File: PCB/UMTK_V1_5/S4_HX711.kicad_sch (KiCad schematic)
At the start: 13 parts, among them Q9 Q_PNP_BEC, U1 HX711

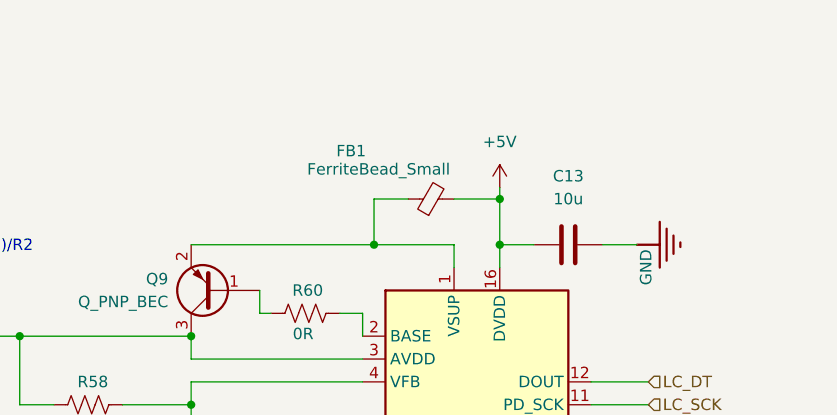
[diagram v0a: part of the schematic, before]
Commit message: Updated Schematics
Done: 7 Seg, Power, Motor, Slide, HX711
To Do: Arduino
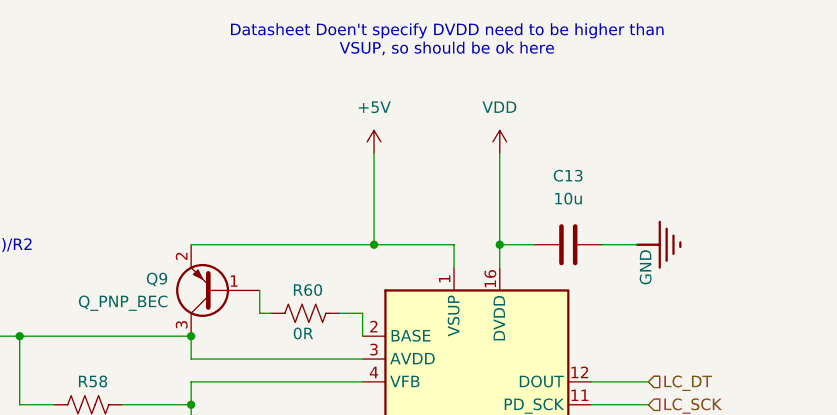
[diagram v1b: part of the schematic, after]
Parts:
- removed FB1: FerriteBead_Small, symbol Device:FerriteBead_Small
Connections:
- net +5V: now also Q9.2 (E), U1.1 (VSUP); no longer C13.1, U1.16 (DVDD)
- new net VDD: C13.1, U1.16 (DVDD)
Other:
- note added: "Datasheet Doen't specify DVDD need to be higher than VSUP, so should be ok here"
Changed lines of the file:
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@@
 	(paper "A4")
-	(junction
-		(at 167.64 82.55)
-		(diameter 0)
-		(color 0 0 0 0)
-	)
 	(junction
 		(at 115.57 127)
@@
 	(wire
 		(pts
-			(xy 167.64 82.55) (xy 167.64 87.63)
-		)
-		(stroke
-			(width 0)
-			(type default)
-		)
-	)
-	(wire
-		(pts
 			(xy 146.05 113.03) (xy 152.4 113.03)
 		)
@@
 	(wire
 		(pts
-			(xy 157.48 82.55) (xy 153.67 82.55)
-		)
-		(stroke
-			(width 0)
-			(type default)
-		)
-	)
-	(wire
-		(pts
 			(xy 88.9 97.79) (xy 100.33 97.79)
 		)
@@
 	(wire
 		(pts
-			(xy 162.56 82.55) (xy 167.64 82.55)
-		)
-		(stroke
-			(width 0)
-			(type default)
-		)
-	)
-	(wire
-		(pts
-			(xy 167.64 81.28) (xy 167.64 82.55)
+			(xy 153.67 77.47) (xy 153.67 87.63)
 		)
 		(stroke
@@
 	(wire
 		(pts
-			(xy 153.67 82.55) (xy 153.67 87.63)
-		)
-		(stroke
-			(width 0)
-			(type default)
-		)
-	)
-	(wire
-		(pts
 			(xy 167.64 87.63) (xy 171.45 87.63)
 		)
@@
 		(pts
 			(xy 179.07 87.63) (xy 182.88 87.63)
+		)
+		(stroke
+			(width 0)
+			(type default)
+		)
+	)
+	(wire
+		(pts
+			(xy 167.64 77.47) (xy 167.64 87.63)
 		)
 		(stroke
@@
 			)
 			(justify left)
+		)
+	)
+	(text "Datasheet Doen't specify DVDD need to be higher than \nVSUP, so should be ok here"
+		(exclude_from_sim no)
+		(at 161.798 65.024 0)
+		(effects
+			(font
+				(size 1.27 1.27)
+			)
 		)
 	)
@@
 	)
 	(symbol
-		(lib_id "Device:FerriteBead_Small")
-		(at 160.02 82.55 90)
+		(lib_id "power:VDD")
+		(at 167.64 77.47 0)
 		(unit 1)
 		(exclude_from_sim no)
@@
 		(on_board yes)
 		(dnp no)
-		(property "Reference" "FB1"
-			(at 151.13 77.216 90)
-			(effects
-				(font
-					(size 1.27 1.27)
-				)
-			)
-		)
-		(property "Value" "FerriteBead_Small"
-			(at 154.178 79.248 90)
+		(fields_autoplaced yes)
+		(property "Reference" "#PWR041"
+			(at 167.64 81.28 0)
+			(effects
+				(font
+					(size 1.27 1.27)
+				)
+				(hide yes)
+			)
+		)
+		(property "Value" "VDD"
+			(at 167.64 72.39 0)
 			(effects
 				(font
@@
 		)
 		(property "Footprint" ""
-			(at 160.02 84.328 90)
-			(effects
-				(font
-					(size 1.27 1.27)
-				)
-				(hide yes)
-			)
-		)
-		(property "Datasheet" "~"
-			(at 160.02 82.55 0)
-			(effects
-				(font
-					(size 1.27 1.27)
-				)
-				(hide yes)
-			)
-		)
-		(property "Description" "Ferrite bead, small symbol"
-			(at 160.02 82.55 0)
-			(effects
-				(font
-					(size 1.27 1.27)
-				)
-				(hide yes)
-			)
-		)
-		(pin "2"
+			(at 167.64 77.47 0)
+			(effects
+				(font
+					(size 1.27 1.27)
+				)
+				(hide yes)
+			)
+		)
+		(property "Datasheet" ""
+			(at 167.64 77.47 0)
+			(effects
+				(font
+					(size 1.27 1.27)
+				)
+				(hide yes)
+			)
+		)
+		(property "Description" "Power symbol creates a global label with name \"VDD\""
+			(at 167.64 77.47 0)
+			(effects
+				(font
+					(size 1.27 1.27)
+				)
+				(hide yes)
+			)
 		)
 		(pin "1"
@@
 			(project ""
 				(path "/2bf3ea67-58b8-47b3-a768-ea6950b40edf/b421850b-f091-436d-99dc-672cc95b7600"
-					(reference "FB1")
+					(reference "#PWR041")
 					(unit 1)
 				)
@@
 	(symbol
 		(lib_id "power:+5V")
-		(at 167.64 81.28 0)
+		(at 153.67 77.47 0)
 		(unit 1)
 		(exclude_from_sim no)
@@
 		(fields_autoplaced yes)
 		(property "Reference" "#PWR0142"
-			(at 167.64 85.09 0)
+			(at 153.67 81.28 0)
 			(effects
 				(font
@@
 		)
 		(property "Value" "+5V"
-			(at 167.64 76.2 0)
+			(at 153.67 72.39 0)
 			(effects
 				(font
@@
 		)
 		(property "Footprint" ""
-			(at 167.64 81.28 0)
+			(at 153.67 77.47 0)
 			(effects
 				(font
@@
 		)
 		(property "Datasheet" ""
-			(at 167.64 81.28 0)
+			(at 153.67 77.47 0)
 			(effects
 				(font
@@
 		)
 		(property "Description" ""
-			(at 167.64 81.28 0)
-			(effects
-				(font
+			(at 153.67 77.47 0)
+			(effects
+				(font
